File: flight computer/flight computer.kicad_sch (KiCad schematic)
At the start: 66 parts, among them IC1 114993390, IC2 ADXL375BCCZ-RL, J1 SMA-J-P-H-ST-EM1, J2 SMA-J-P-H-ST-EM1, Q1 BSS138, Q2 BSS84, Q3 PMOS, Q4 NMOS, SW1 SW_Push, U1 TPS56A37RPAR, U2 BMP581, U3 BNO086, U4 BTM9011EP, U5 RP2354B, U6 MAX-M10S-00B, U7 AZ1117CH-3.3TRG1, U8 VND9025AJTR, U9 74LVC1G07GW_125

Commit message: VND9025 high-side switch added
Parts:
- added C27: 0.1uF, Capacitor_SMD:C_0805_2012Metric_Pad1.18x1.45mm_HandSolder, symbol Device:C
- added D4: D, symbol Device:D
- added R17: 4.7k, symbol Device:R
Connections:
- net +12V: now also U8.17 (VCC), C27.1
- net GND: now also C27.2, D4.1 (K), R17.2
- net VND9025 IN0: now reaches U8.1 (INPUT0)
- net +12V Motors: now reaches U8.10 (OUTPUT1)
- net +12V Motors: now also U8.11 (OUTPUT1), U8.12 (OUTPUT1), U8.9 (OUTPUT1)
- net +12V Pyros: now reaches U8.13 (OUTPUT0)
- net +12V Pyros: now also U8.14 (OUTPUT0), U8.15 (OUTPUT0), U8.16 (OUTPUT0)
- net VND9025 FAULT: now reaches U8.2 (*FaultRST)
- net at U8.4 (GND): now also D4.2 (A), R17.1
- net VND9025 IN1: now reaches U8.8 (INPUT1)
- no-connect marks 16 -> 20
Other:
- moved on the sheet: C25, C26, Reference: IC2, Reference: U8

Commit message: Buzzer added
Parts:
- added LS1: CPT-1203-78-SMT-TR, Snapeda:XDCR_CPT-1203-78-SMT-TR, symbol Snapeda:CPT-1203-78-SMT-TR
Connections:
- net GND: now also LS1.2
- new net buzzer: LS1.1
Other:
- moved on the sheet: C27, D4, R17, Reference: U8

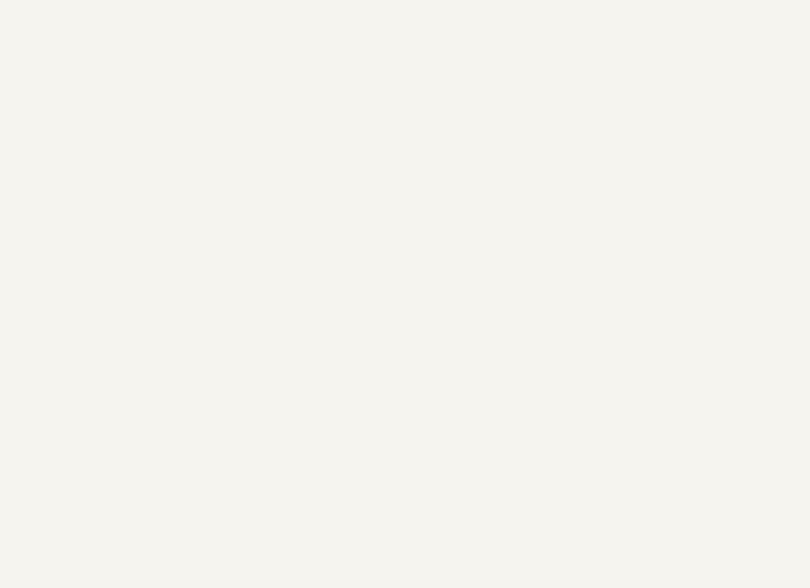
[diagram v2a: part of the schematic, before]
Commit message: Reverse polarity protection added
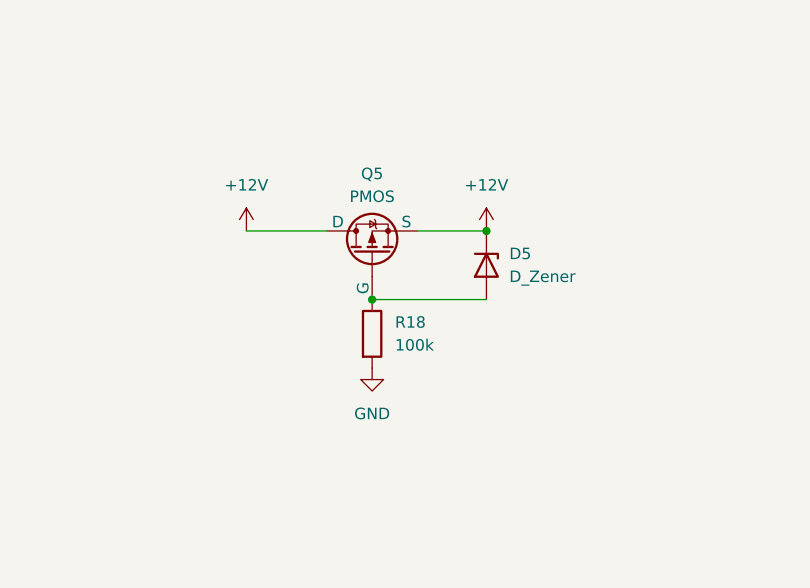
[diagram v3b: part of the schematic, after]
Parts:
- added D5: D_Zener, symbol Device:D_Zener
- added Q5: PMOS, symbol Simulation_SPICE:PMOS
- added R18: 100k, symbol Device:R
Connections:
- net +12V: now also D5.1 (K), Q5.1 (D), Q5.3 (S)
- net GND: now also R18.2
- new net: D5.2 (A), Q5.2 (G), R18.1

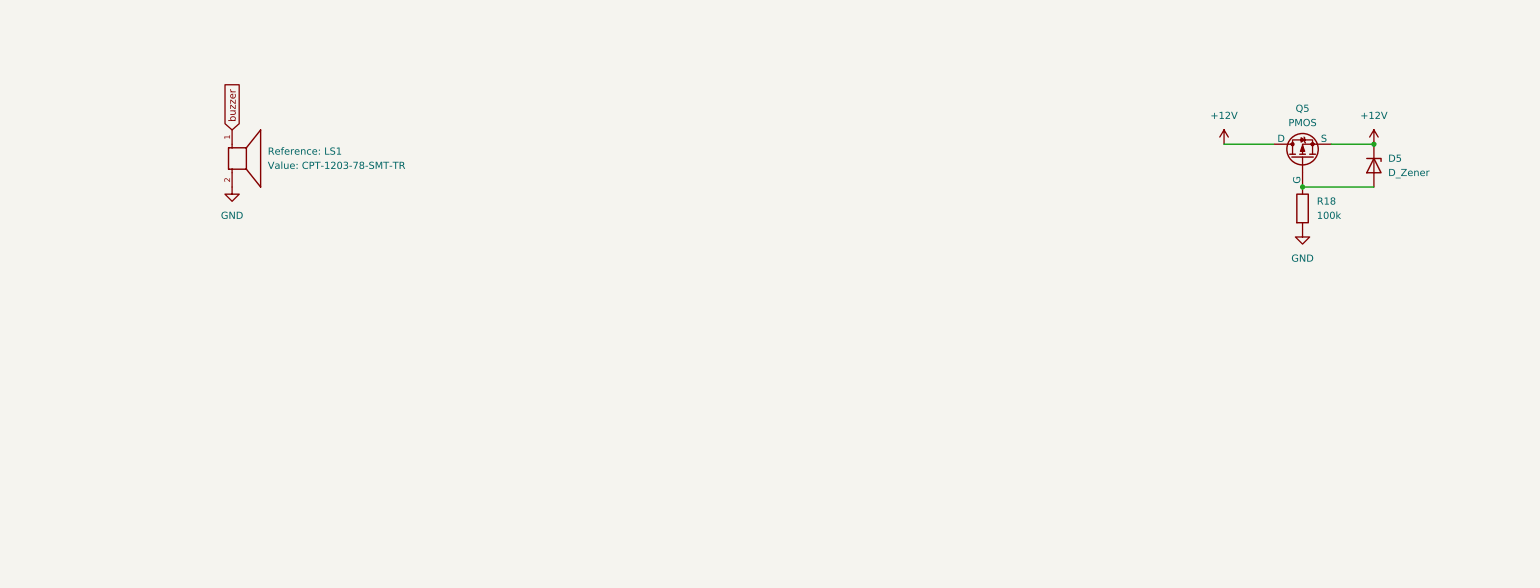
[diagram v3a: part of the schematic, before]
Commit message: TVS diode added
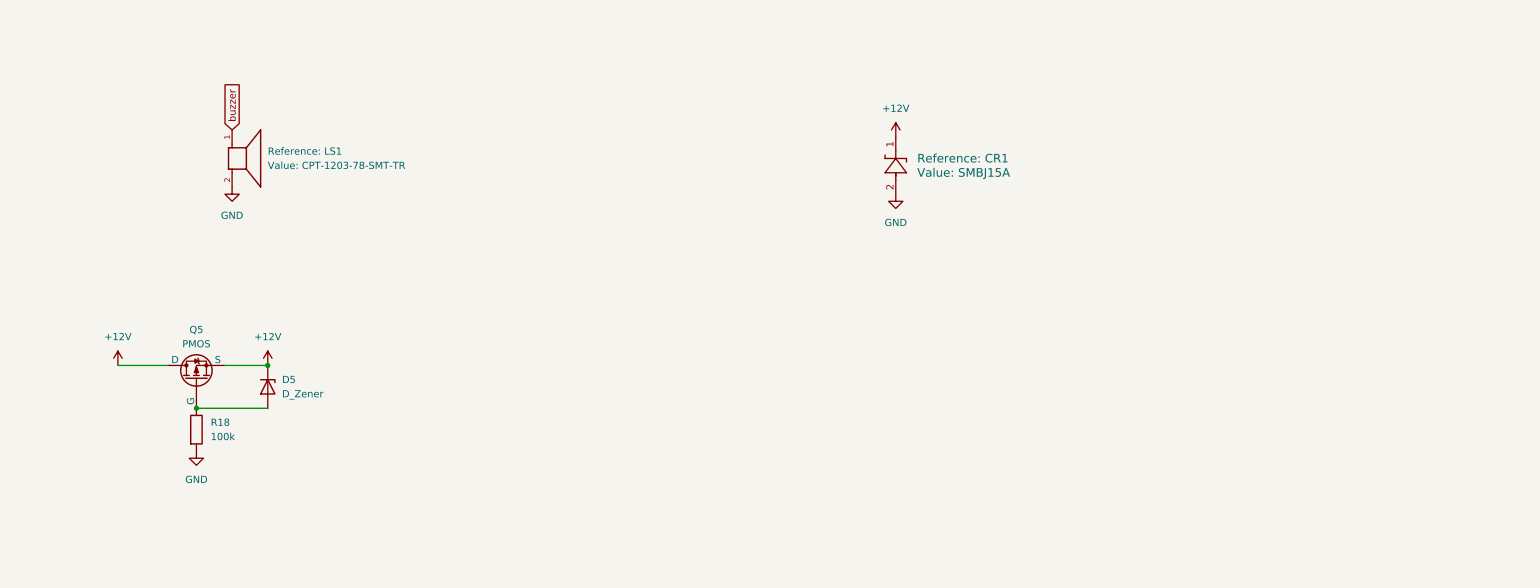
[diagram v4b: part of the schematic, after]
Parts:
- added CR1: SMBJ15A, Snapeda:DO-214AASMB_J-BEND_LTF-L, symbol Snapeda:SMBJ15A
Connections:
- net +12V: now also CR1.1
- net GND: now also CR1.2
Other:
- moved on the sheet: D5, Q5, R18

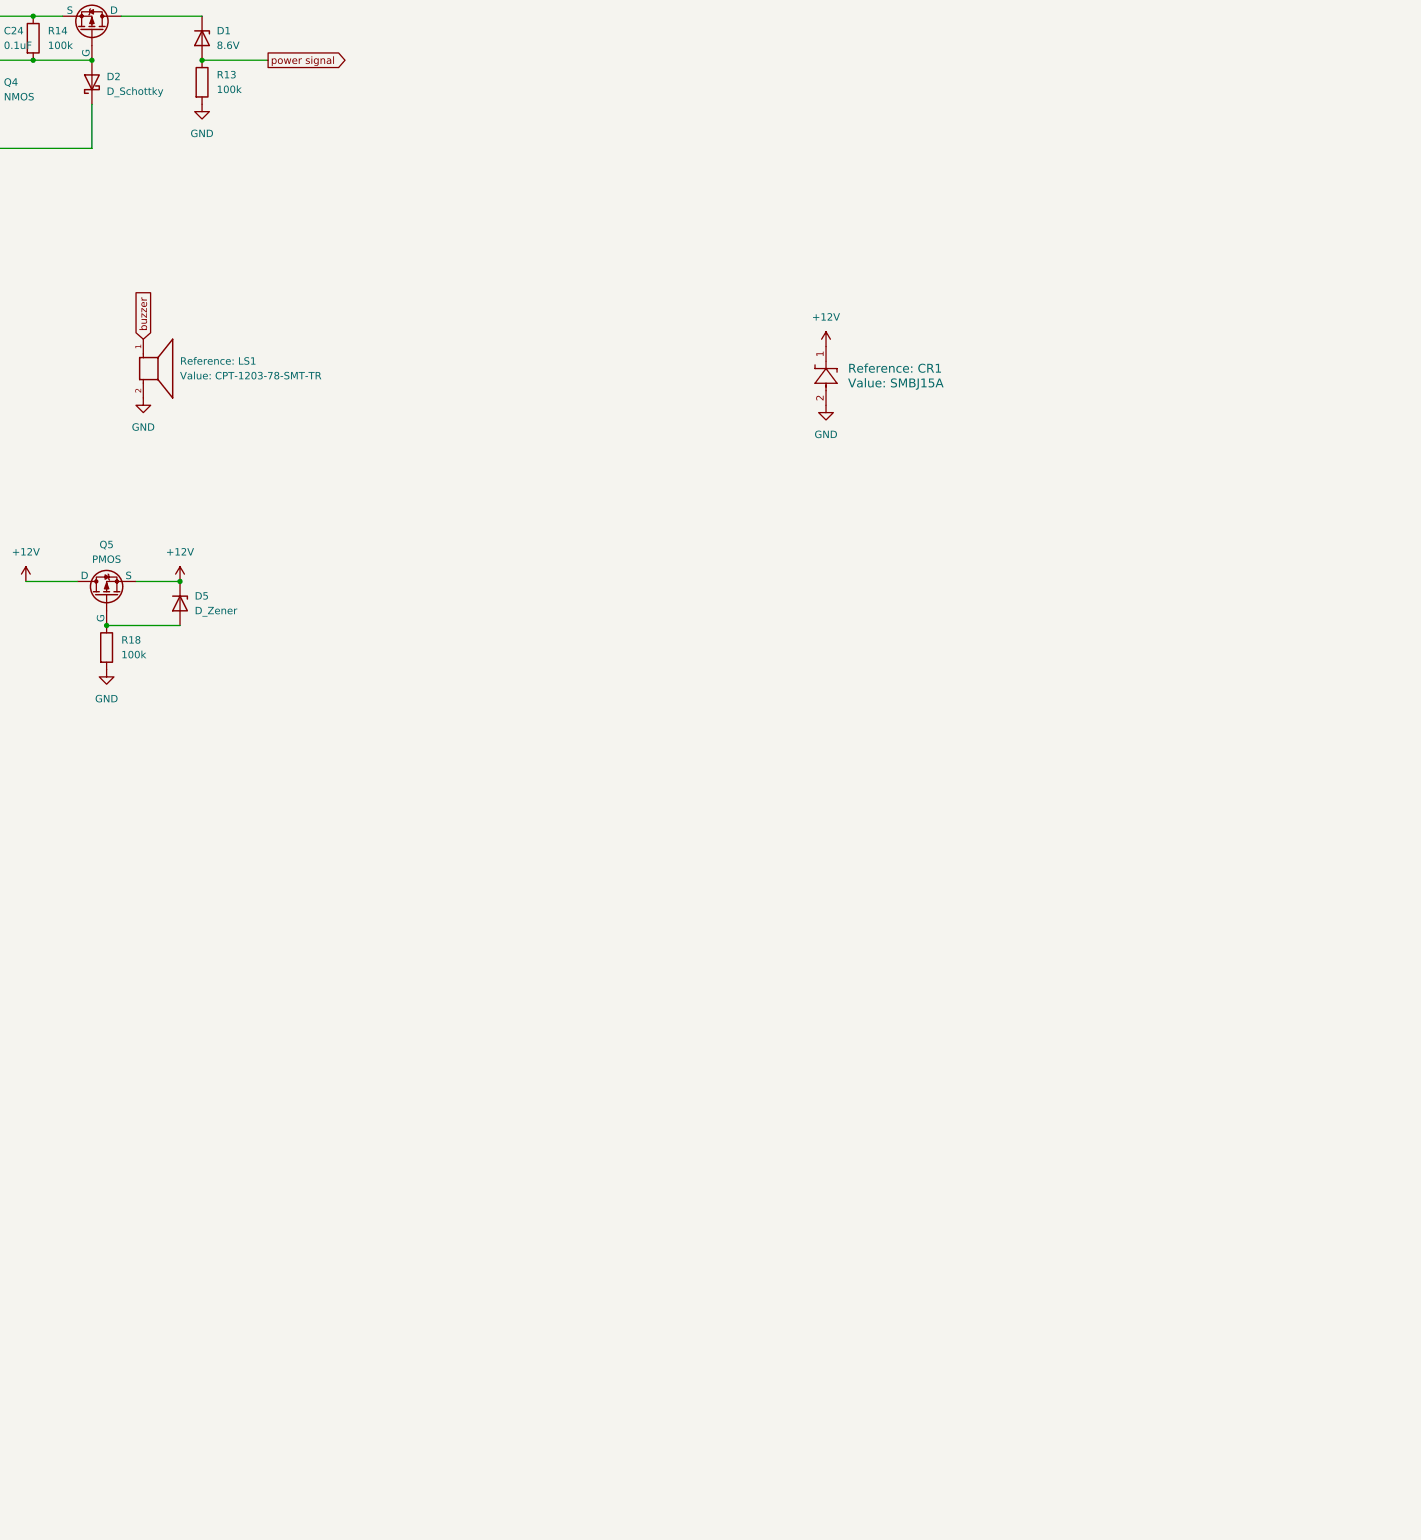
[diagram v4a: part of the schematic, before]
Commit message: SD card added
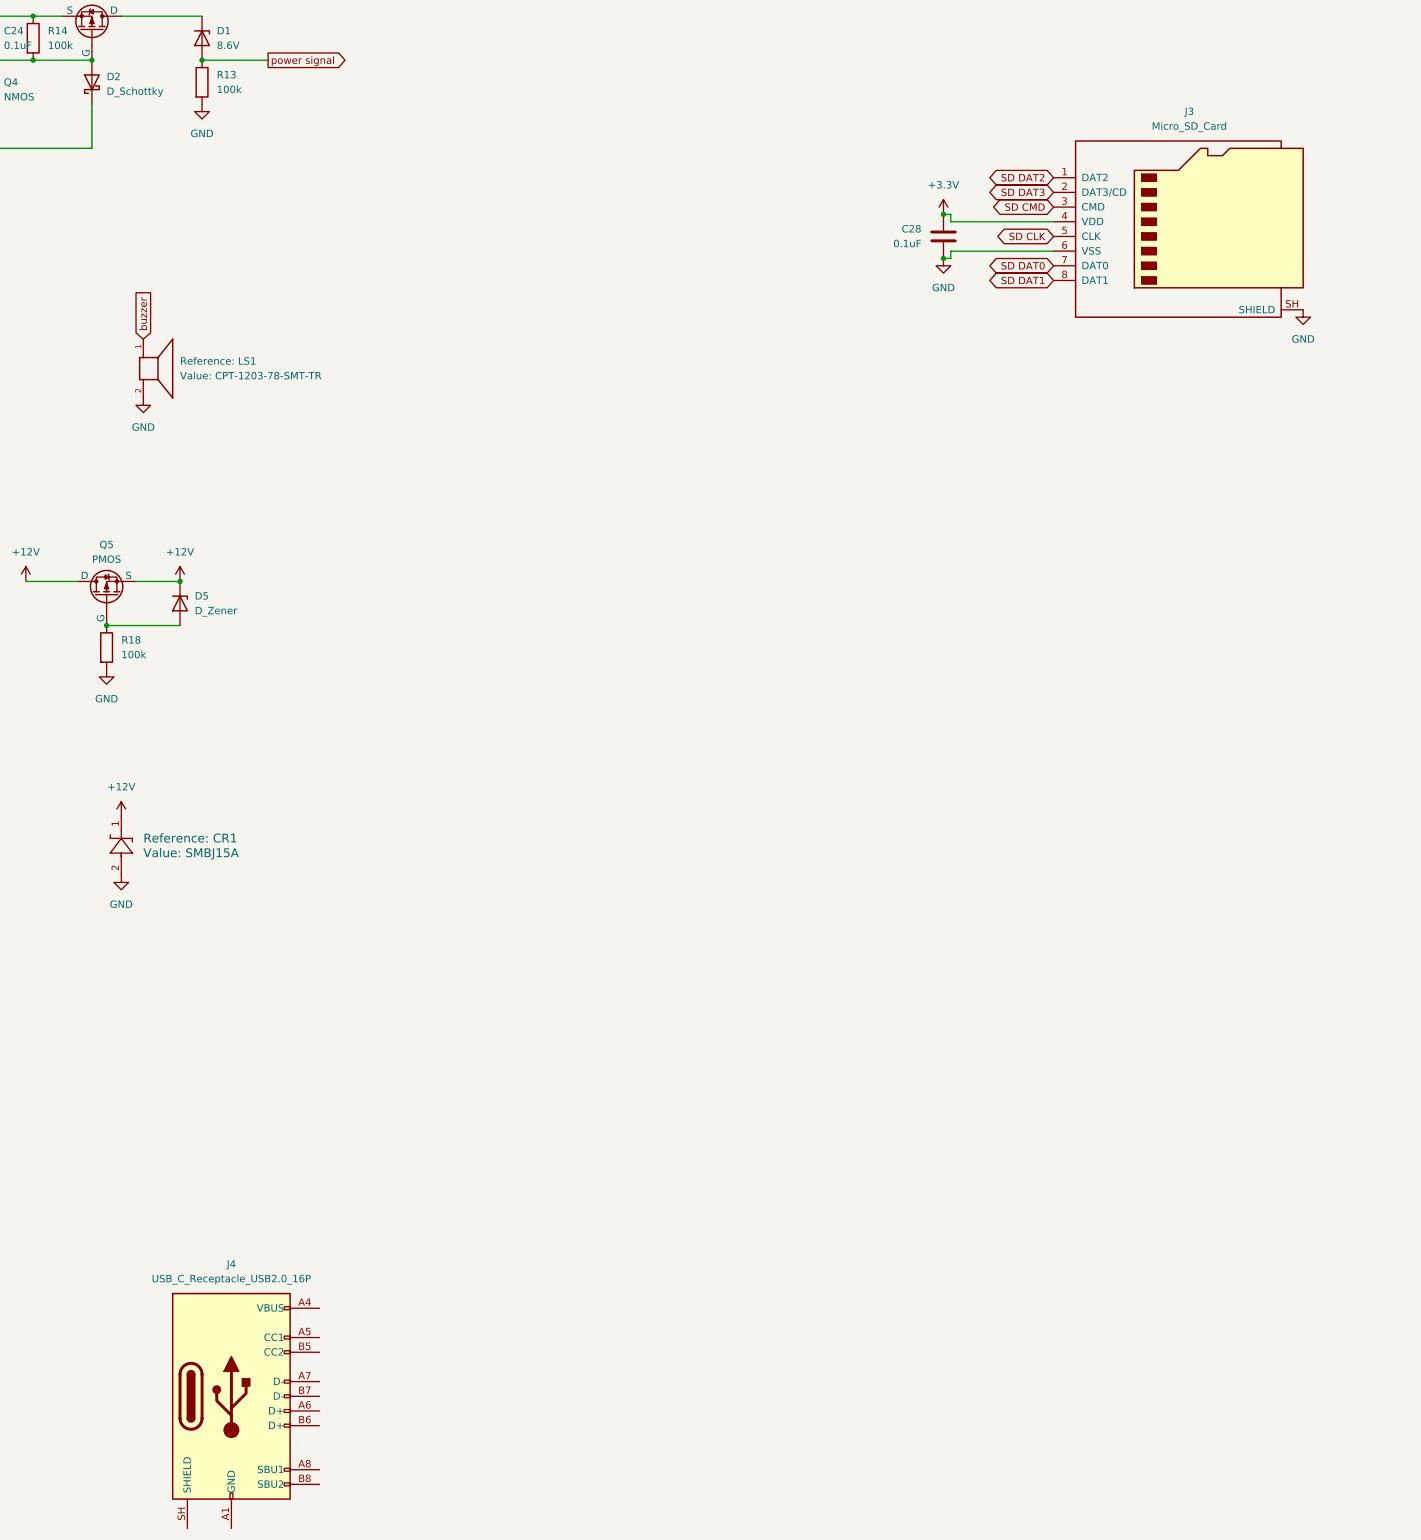
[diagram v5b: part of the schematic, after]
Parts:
- added C28: 0.1uF, Capacitor_SMD:C_0805_2012Metric_Pad1.18x1.45mm_HandSolder, symbol Device:C
- added J3: Micro_SD_Card, Connector_Card:microSD_HC_Molex_47219-2001, symbol Connector:Micro_SD_Card
- added J4: USB_C_Receptacle_USB2.0_16P, Connector_USB:USB_C_Receptacle_GCT_USB4105-xx-A_16P_TopMnt_Horizontal, symbol Connector:USB_C_Receptacle_USB2.0_16P
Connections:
- net +3.3V: now also C28.1, J3.4 (VDD)
- net GND: now also C28.2, J3.6 (VSS), J3.SH (SHIELD)
- new net: J4.A1 (GND), J4.A12 (GND), J4.B1 (GND), J4.B12 (GND)
- new net: J4.A4 (VBUS), J4.A9 (VBUS), J4.B4 (VBUS), J4.B9 (VBUS)
- new net SD CLK: J3.5 (CLK)
- new net SD CMD: J3.3 (CMD)
- new net SD DAT0: J3.7 (DAT0)
- new net SD DAT1: J3.8 (DAT1)
- new net SD DAT2: J3.1 (DAT2)
- new net SD DAT3: J3.2 (DAT3/CD)
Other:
- moved on the sheet: Reference: CR1

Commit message: USB C added
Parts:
- added D6: D_Schottky, symbol Device:D_Schottky
- added R19, R20: 5.1k, symbol Device:R
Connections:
- net +5V: now also D6.1 (K)
- net GND: now also J4.A1 (GND), J4.A12 (GND), J4.B1 (GND), J4.B12 (GND), J4.SH (SHIELD), R19.2, R20.2
- net at J4.A4 (VBUS), J4.A9 (VBUS), J4.B4 (VBUS)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: now also D6.2 (A)
- net at J4.A5 (CC1): now also R19.1
- net USB_D+: now reaches J4.A6 (D+)
- net USB_D+: now also J4.B6 (D+)
- net USB_D-: now reaches J4.A7 (D-)
- net USB_D-: now also J4.B7 (D-)
- net at J4.B5 (CC2): now also R20.1
- no-connect marks 20 -> 22
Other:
- moved on the sheet: C1, C10, C14, C15, C16, C17, C2, C22, C23, C28, C3, C4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

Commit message: Pyro MOSFETs added
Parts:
- added Q6: DMN3016LFDE-7, Samacsys:DMP25H18DLFDE7, symbol Samacsys:DMN3016LFDE-7
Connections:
- net GND: now also Q6.1 (D_1), Q6.2 (D_2), Q6.5 (D_3), Q6.6 (D_4), Q6.8 (D_5)
- new net PYRO_1 gate: Q6.3 (G)
- new net PYRO_1 source: Q6.4 (S_1), Q6.7 (S_2)
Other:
- moved on the sheet: D6, J4, R19, R20, U5

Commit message: LEDs added
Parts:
- removed Q6: DMN3016LFDE-7, Samacsys:DMP25H18DLFDE7, symbol Samacsys:DMN3016LFDE-7
- removed SW1: SW_Push, symbol Switch:SW_Push
- added R21, R22, R23, R24, R25, R26, R27: 110, symbol Device:R
- added R28: 330, symbol Device:R
- added U10: SIA440DJ-T1-GE3, Snapeda:SON_1DJ-T1-GE3_VIS, symbol Snapeda:SIA440DJ-T1-GE3
- added U11: high, Snapeda:LTST-BILED-15X16, symbol Snapeda:LTST-C195KGJRKT
- added U12: medium, Snapeda:LTST-BILED-15X16, symbol Snapeda:LTST-C195KGJRKT
- added U13: low, Snapeda:LTST-BILED-15X16, symbol Snapeda:LTST-C195KGJRKT
- added U14: power, Snapeda:LTST-BILED-15X16, symbol Snapeda:LTST-C195KGJRKT
- added U15: fault, Snapeda:LTST-BILED-15X16, symbol Snapeda:LTST-C195KGJRKT
- added U16: JS207011SCQNR, Snapeda:SOIC_SCQNR_CNK, symbol Snapeda:JS207011SCQNR
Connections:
- net +5V: now also R28.1
- net GND: now also U10.1, U10.2, U10.5, U10.6, U11.P$3, U11.P$4, U12.P$3, U12.P$4, U13.P$3, U13.P$4, U14.P$3, U14.P$4, U15.P$3, U15.P$4, U16.1, U16.5
- net PYRO_1 gate: now also U10.3
- net PYRO_1 source: now also U10.4, U10.7
- net at D2.1 (K), D3.1 (K): now also U16.3, U16.7
- new net: R21.2, U11.P$1
- new net: R22.2, U11.P$2
- new net: R25.2, U13.P$1
- new net: R28.2, U14.P$1
- new net: R26.2, U13.P$2
- new net: R27.2, U15.P$1
- new net: R24.2, U12.P$2
- new net: R23.2, U12.P$1
- new net LED fault: R27.1
- new net LED high green: R21.1
- new net LED high red: R22.1
- new net LED low green: R25.1
- new net LED low red: R26.1
- new net LED medium green: R23.1
- new net LED medium red: R24.1
- no-connect marks 22 -> 28
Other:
- moved on the sheet: C24, D1, D2, D3, Q3, Q4, R13, R14, R15, R16
